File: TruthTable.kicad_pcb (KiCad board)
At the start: 2 copper layers, 20 x 110 mm, 26 parts, among them J1 Conn_02x05_Odd_Even, SW1 SW_SPDT, SW2 SW_SPDT, SW3 SW_SPDT, SW4 SW_SPDT, SW5 SW_SPDT, SW6 SW_SPDT, SW7 SW_SPDT, SW8 SW_SPDT, U1 74HC14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

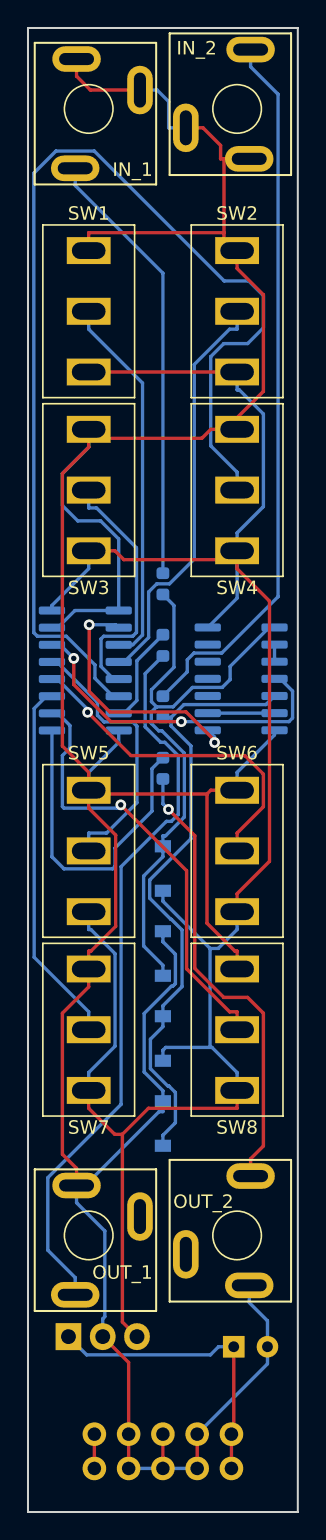
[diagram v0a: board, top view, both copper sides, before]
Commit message: Updated labels
Updated labels in the schematic to match the final naming scheme used on the panel
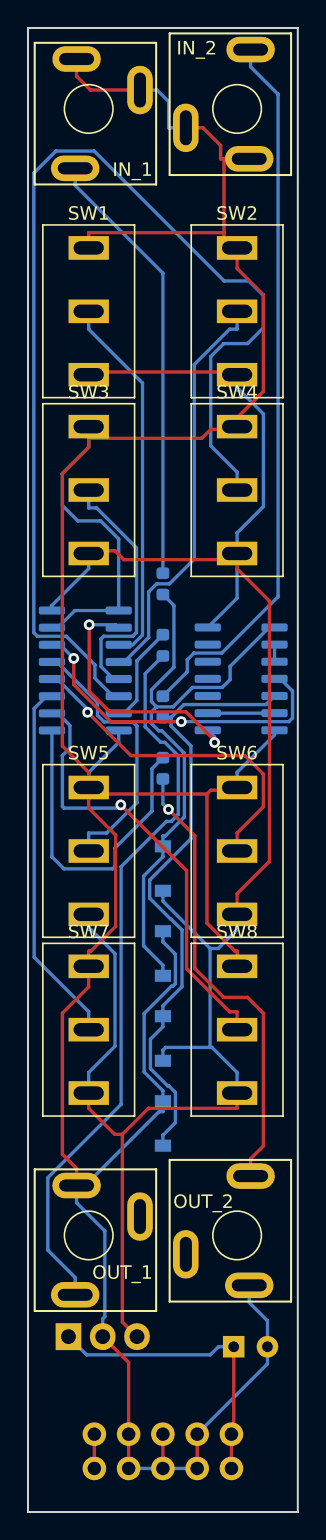
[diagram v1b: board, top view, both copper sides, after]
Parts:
- SW1, SW2, SW3, SW4, SW5, SW6, SW7, SW8: footprint Attoparsec:ANT11SEBQE-SPDT -> Attoparsec:54-302PC_SPDT
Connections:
- net TRUTH_A_1 renamed TRUTH_1_A_B
- net TRUTH_A_2 renamed TRUTH_1_NA_B
- net TRUTH_A_3 renamed TRUTH_1_A_NB
- net TRUTH_A_4 renamed TRUTH_1_NA_NB
- net TRUTH_B_1 renamed TRUTH_2_A_B
- net TRUTH_B_2 renamed TRUTH_2_NA_B
- net TRUTH_B_3 renamed TRUTH_2_A_NB
- net TRUTH_B_4 renamed TRUTH_2_NA_NB
